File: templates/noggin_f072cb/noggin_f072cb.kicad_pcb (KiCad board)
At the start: 2 copper layers, 32 parts, among them J1 CAN, J2 CAN, J3 SWD_UART, SW1 DBG2, SW2 DBG1, SW3 RST, U1 STM32F072CBUx, U2 AZ1117-3.3, U3 ATA6561

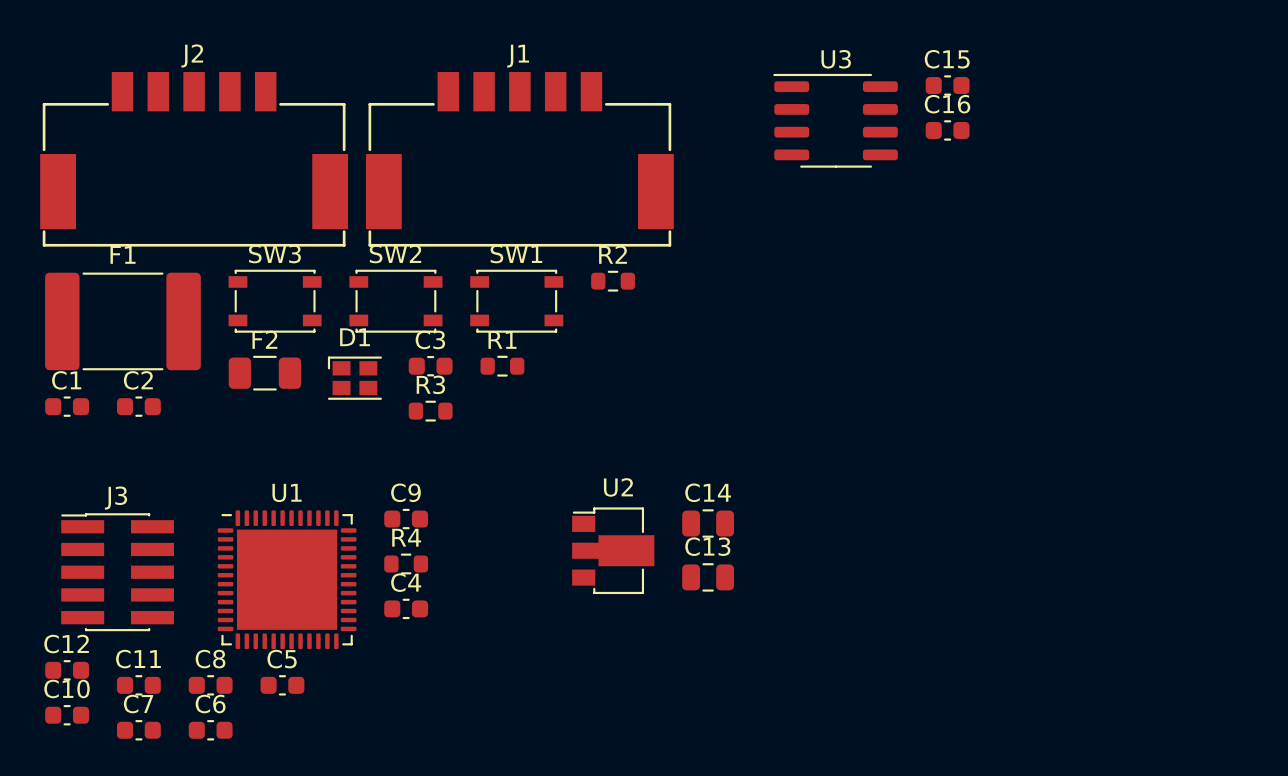
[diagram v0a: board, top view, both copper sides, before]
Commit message: Refactor and update templates
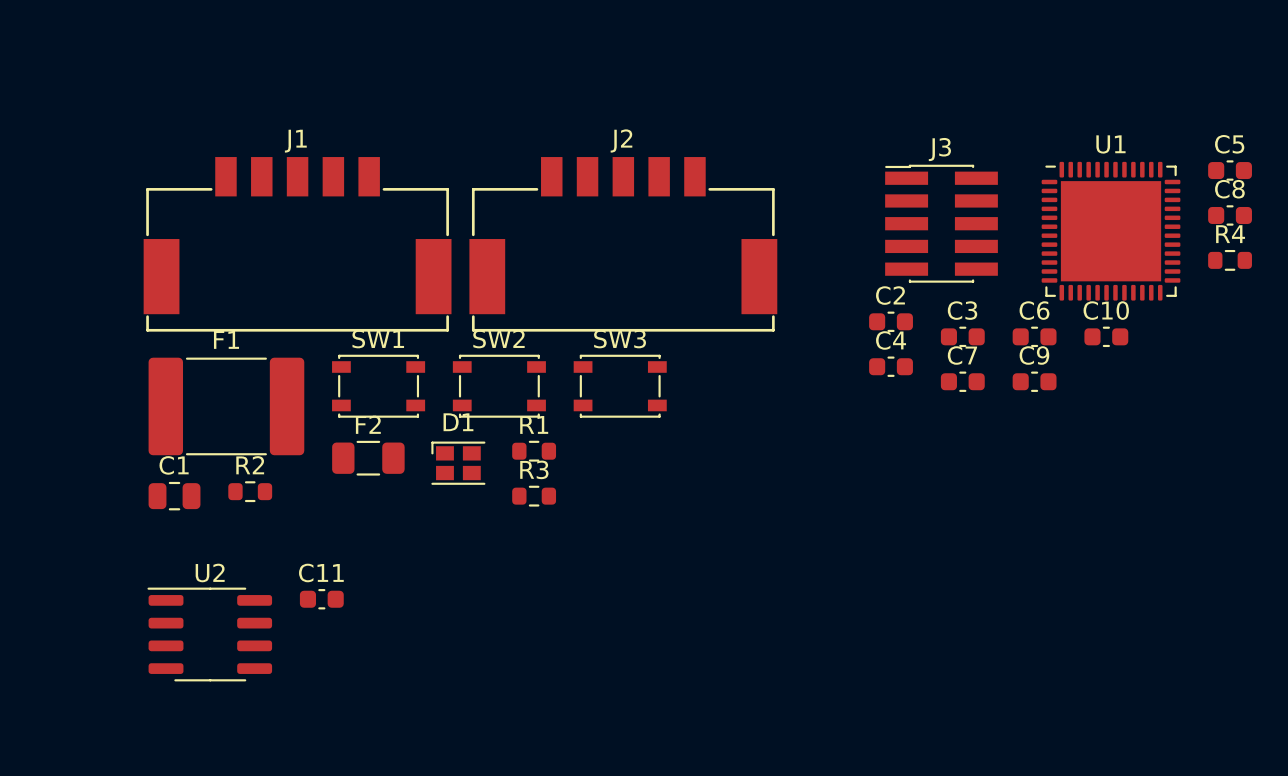
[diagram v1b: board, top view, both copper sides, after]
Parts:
- removed C12, C15, C16: 100n, Capacitor_SMD:C_0603_1608Metric
- removed C13, C14: 10u, Capacitor_SMD:C_0805_2012Metric
- removed U3: ATA6561, Package_SO:SOIC-8_3.9x4.9mm_P1.27mm
- C1: value 100n -> 10u; footprint Capacitor_SMD:C_0603_1608Metric -> Capacitor_SMD:C_0805_2012Metric
- C11: value 1u -> 100n
- C3: value 100n -> 1u
- U2: value AZ1117-3.3 -> TCAN330G; footprint Package_TO_SOT_SMD:SOT-89-3 -> Package_SO:SOIC-8_3.9x4.9mm_P1.27mm
- moved C8 62.7 mm to (185.0, 90.8)
- moved C10 61.8 mm to (178.1, 97.6)
- moved C5 60.2 mm to (185.0, 88.3)
- moved C6 51.0 mm to (174.1, 97.6)
- moved J3 50.0 mm to (168.8, 91.3)
- moved U1 50.0 mm to (178.3, 91.7)
- moved C7 50.0 mm to (170.0, 100.1)
- moved R4 49.1 mm to (185.0, 93.3)
- moved C2 42.3 mm to (166.0, 96.8)
- moved C9 35.9 mm to (174.1, 100.1)
- moved C4 30.3 mm to (166.0, 99.3)
- moved C3 29.8 mm to (170.0, 97.6)
- moved J2 24.4 mm to (151.1, 97.2)
- moved R2 23.4 mm to (130.2, 106.2)
- moved U2 23.0 mm to (128.0, 114.2)
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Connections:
- C1 pad 1: /DBG2 -> +3V3
- C2 pad 1: /DBG1 -> /RST
- C3 pad 1: /RST -> +3V3
- C4 pad 1: /RST -> +3V3
- F2 pad 1: +5V -> +3V3
- U2 pad 1: GND -> /CAN_TX
- U2 pad 2: +3V3 -> GND
- U2 pad 3: +5V -> +3V3
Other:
- net class Default: via_dia 0.5588 -> 0.6096; via_drill 0.254 -> 0.3048
- rule via_min_size: 0.5588 -> 0.508

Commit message: convert to kicad 6
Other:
- net class Default removed
